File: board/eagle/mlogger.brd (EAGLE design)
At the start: 59.4 x 33.3 mm, 47 parts, among them J1 MICROSD-9P, SW1 SS-12D00G3, SW2 TVAF06-A020B-R, SW3 TVAF06-A020B-R

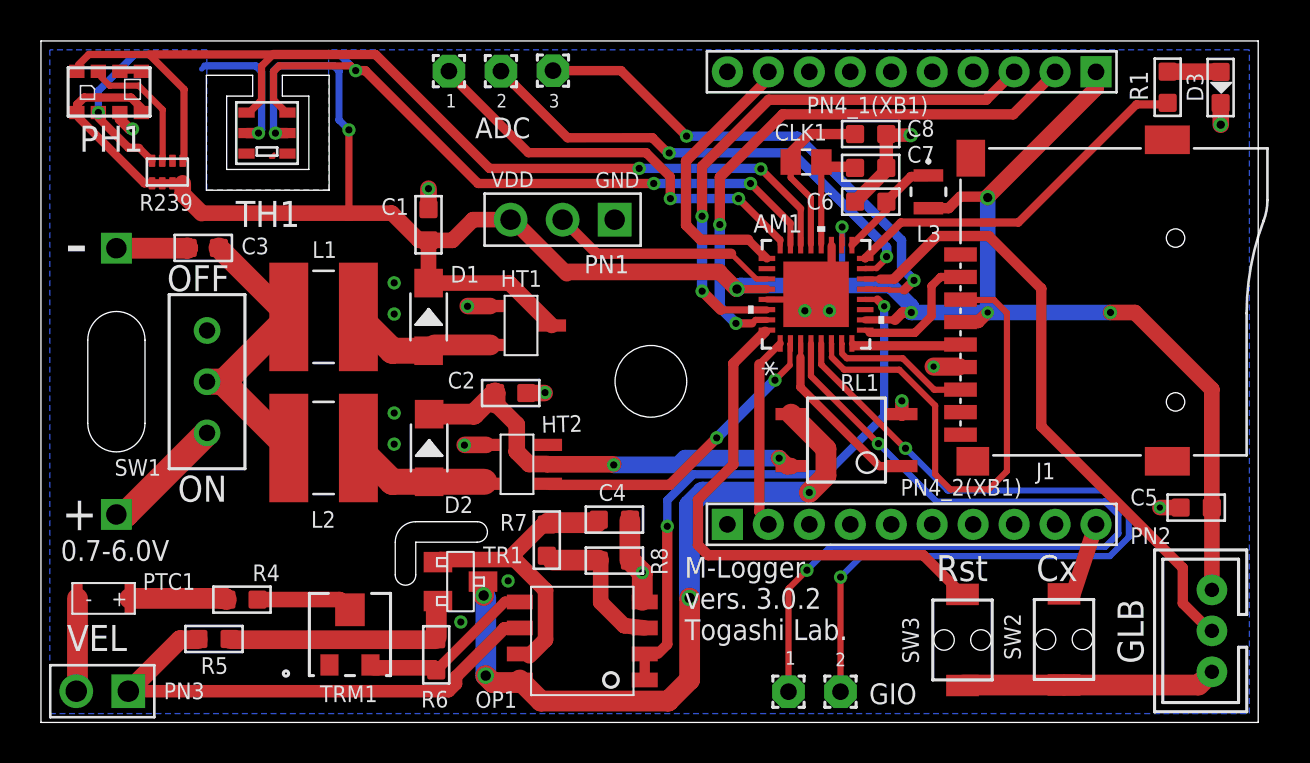
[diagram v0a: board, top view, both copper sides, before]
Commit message: UPDI, GAD名称設定。 ノイズ対策で配線間隔を拡大。
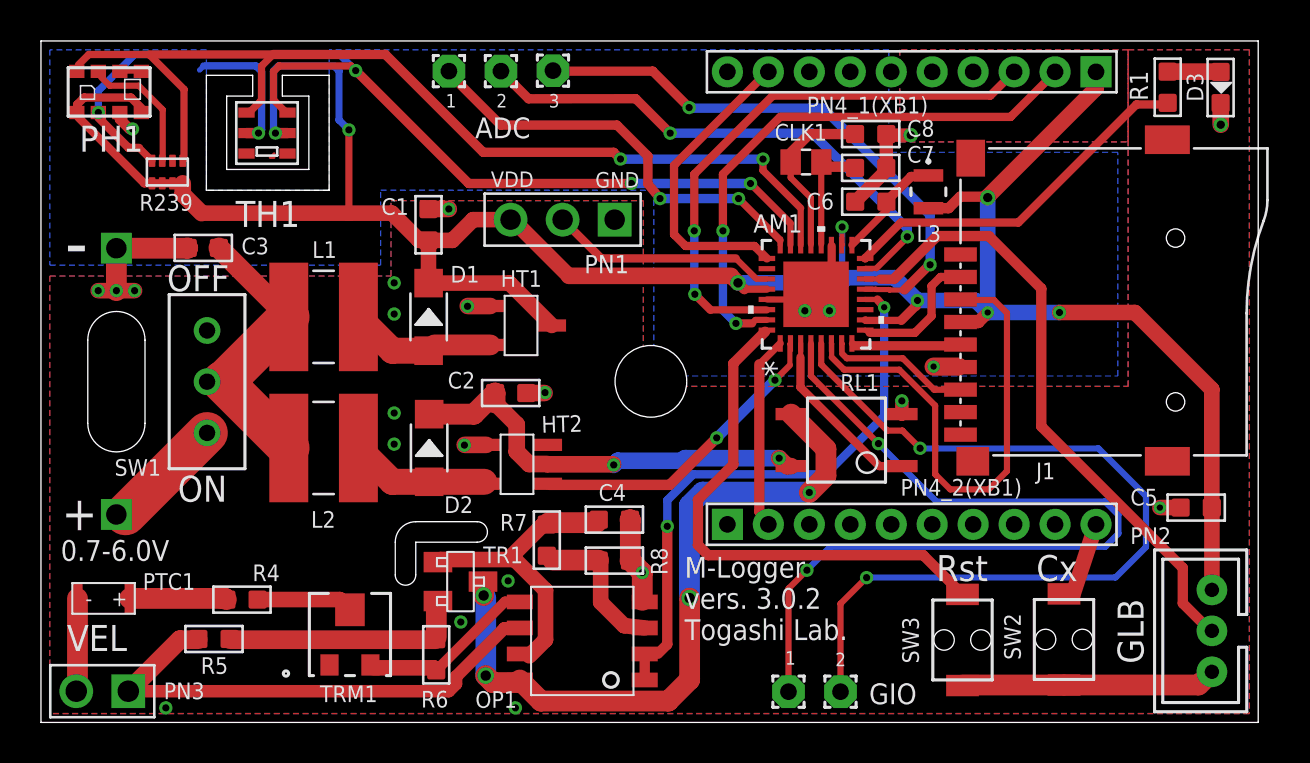
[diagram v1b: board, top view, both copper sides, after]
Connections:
- net N$11 renamed GADC2
- net N$7 renamed UPDI
- net N$8 renamed GADC3
- net N$9 renamed GADC1
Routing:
- net GND: track 52.4 -> 56.3 mm, vias 20 -> 25
- net GADC3: track 25.3 -> 27.5 mm
- net GADC2: track 24.2 -> 26.2 mm
- net N$12: track 40.7 -> 42.4 mm
- net SLP: track 13.8 -> 14.9 mm
- net TXD: track 26.8 -> 27.4 mm
- added copper zone on layer 1, net GND

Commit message: 表面にもベタGNDを追加。 TXD, RXDなどの間にGNDガードを追加。
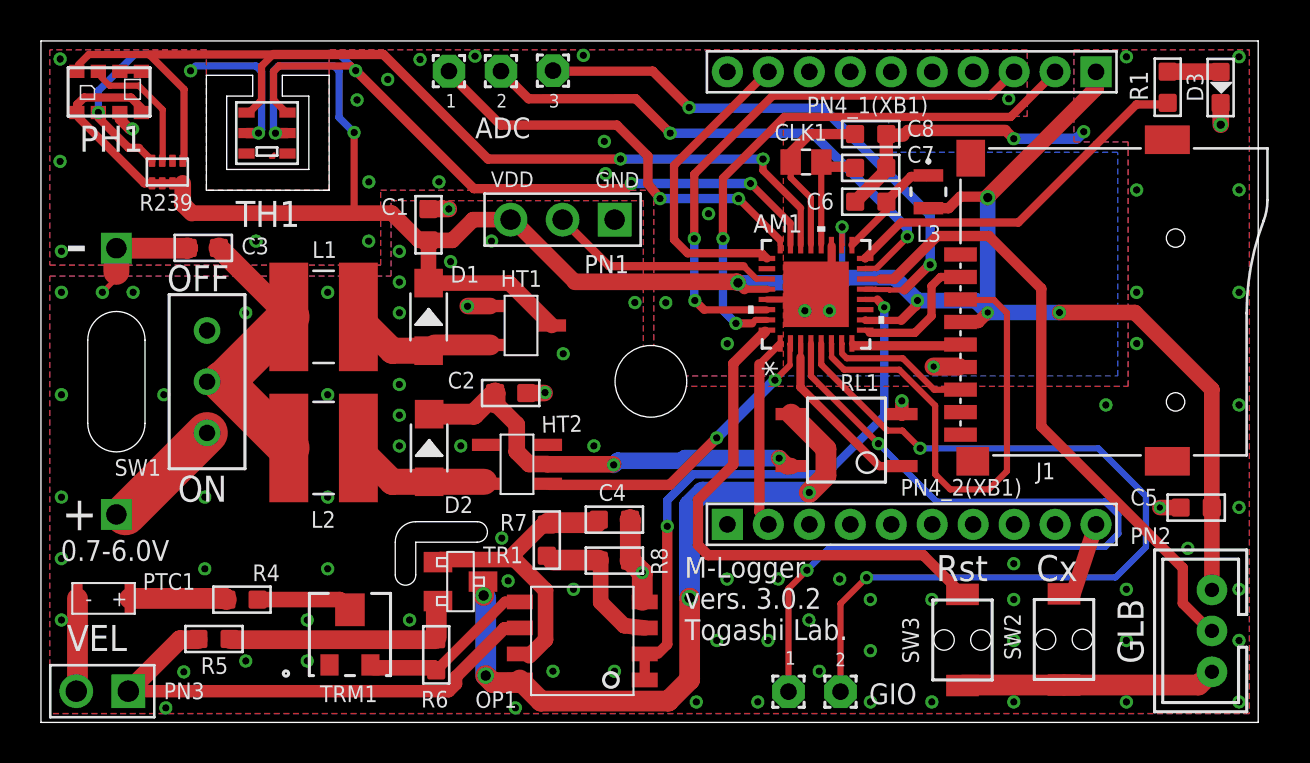
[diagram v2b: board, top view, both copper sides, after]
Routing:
- net GND: track 56.3 -> 63.1 mm, vias 25 -> 107
